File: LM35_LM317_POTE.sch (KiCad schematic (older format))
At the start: 21 parts, among them J10 TB_1X2, J6 TB_1X2, J7 TB_1X2, J8 TB_1X2, J9 TB_1X2, P4 CONN_01X03, P5 CONN_02X02, P6 CONN_01X02, P7 CONN_01X02, P8 CONN_01X02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

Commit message: Ruteo del PCB, agrego una salida de 5v y 3v en el esquematico
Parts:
- J10: value TB_1X2 -> PotO.Out
- J6: value TB_1X2 -> V.RegOut
- J7: value TB_1X2 -> Temp.Out
- J8: value TB_1X2 -> C.RegOut
- J9: value TB_1X2 -> PotTOut
- P4: value CONN_01X03 -> Pot2_Out
- P5: value CONN_02X02 -> C.reg.in
- P6: value CONN_01X02 -> V_regOut
- P7: value CONN_01X02 -> Temp_Out
- P8: value CONN_01X02 -> C_RegOut
- P9: value CONN_01X03 -> PotO_Out
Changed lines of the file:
@@
 $EndComp
 $Comp
-L GND #PWR028
+L GND #PWR031
 U 1 1 581A256F
 P 4800 1450
-F 0 "#PWR028" H 4800 1200 50  0001 C CNN
+F 0 "#PWR031" H 4800 1200 50  0001 C CNN
 F 1 "GND" H 4800 1300 50  0000 C CNN
 F 2 "" H 4800 1450 50  0000 C CNN
@@
 P 5150 1350
 F 0 "P8" H 5150 1500 50  0000 C CNN
-F 1 "CONN_01X02" V 5250 1350 50  0000 C CNN
+F 1 "C_RegOut" V 5250 1350 50  0000 C CNN
 F 2 "Pin_Headers:Pin_Header_Straight_1x02" H 5150 1350 50  0001 C CNN
 F 3 "" H 5150 1350 50  0000 C CNN
@@
 P 1850 1250
 F 0 "P5" H 1850 1400 50  0000 C CNN
-F 1 "CONN_02X02" H 1850 1100 50  0000 C CNN
+F 1 "C.reg.in" H 1850 1100 50  0000 C CNN
 F 2 "Pin_Headers:Pin_Header_Straight_2x02" H 1850 50  50  0001 C CNN
 F 3 "" H 1850 50  50  0000 C CNN
@@
 $EndComp
 $Comp
-L +5V #PWR029
+L +5V #PWR032
 U 1 1 581A2572
 P 1300 1000
-F 0 "#PWR029" H 1300 850 50  0001 C CNN
+F 0 "#PWR032" H 1300 850 50  0001 C CNN
 F 1 "+5V" H 1300 1140 50  0000 C CNN
 F 2 "" H 1300 1000 50  0000 C CNN
@@
 $EndComp
 $Comp
-L +3.3V-RESCUE-ciaa-nxp #PWR030
+L +3.3V-RESCUE-ciaa-nxp #PWR033
 U 1 1 581A2573
 P 950 1000
-F 0 "#PWR030" H 950 850 50  0001 C CNN
+F 0 "#PWR033" H 950 850 50  0001 C CNN
 F 1 "+3.3V" H 950 1140 50  0000 C CNN
 F 2 "" H 950 1000 50  0000 C CNN
@@
 $EndComp
 $Comp
-L GND #PWR031
+L GND #PWR034
 U 1 1 581A2577
 P 4400 3500
-F 0 "#PWR031" H 4400 3250 50  0001 C CNN
+F 0 "#PWR034" H 4400 3250 50  0001 C CNN
 F 1 "GND" H 4400 3350 50  0000 C CNN
 F 2 "" H 4400 3500 50  0000 C CNN
@@
 P 4750 3400
 F 0 "P6" H 4750 3550 50  0000 C CNN
-F 1 "CONN_01X02" V 4850 3400 50  0000 C CNN
+F 1 "V_regOut" V 4850 3400 50  0000 C CNN
 F 2 "Pin_Headers:Pin_Header_Straight_1x02" H 4750 3400 50  0001 C CNN
 F 3 "" H 4750 3400 50  0000 C CNN
@@
 $EndComp
 $Comp
-L +5V #PWR032
+L +5V #PWR035
 U 1 1 581A2579
 P 1700 3150
-F 0 "#PWR032" H 1700 3000 50  0001 C CNN
+F 0 "#PWR035" H 1700 3000 50  0001 C CNN
 F 1 "+5V" H 1700 3290 50  0000 C CNN
 F 2 "" H 1700 3150 50  0000 C CNN
@@
 $EndComp
 $Comp
-L GND #PWR033
+L GND #PWR036
 U 1 1 581A257B
 P 3700 4650
-F 0 "#PWR033" H 3700 4400 50  0001 C CNN
+F 0 "#PWR036" H 3700 4400 50  0001 C CNN
 F 1 "GND" H 3700 4500 50  0000 C CNN
 F 2 "" H 3700 4650 50  0000 C CNN
@@
 P 5600 3400
 F 0 "J6" H 5600 3700 60  0000 C CNN
-F 1 "TB_1X2" H 5650 3100 60  0000 C CNN
+F 1 "V.RegOut" H 5650 3100 60  0000 C CNN
 F 2 "Connect:AK300-2" H 5550 3450 60  0001 C CNN
 F 3 "" H 5550 3450 60  0000 C CNN
@@
 $EndComp
 $Comp
-L GND #PWR034
+L GND #PWR037
 U 1 1 581A257D
 P 5100 3550
-F 0 "#PWR034" H 5100 3300 50  0001 C CNN
+F 0 "#PWR037" H 5100 3300 50  0001 C CNN
 F 1 "GND" H 5100 3400 50  0000 C CNN
 F 2 "" H 5100 3550 50  0000 C CNN
@@
 P 6150 1250
 F 0 "J8" H 6150 1550 60  0000 C CNN
-F 1 "TB_1X2" H 6200 950 60  0000 C CNN
+F 1 "C.RegOut" H 6200 950 60  0000 C CNN
 F 2 "Connect:AK300-2" H 6100 1300 60  0001 C CNN
 F 3 "" H 6100 1300 60  0000 C CNN
@@
 $EndComp
 $Comp
-L GND #PWR035
+L GND #PWR038
 U 1 1 581A257F
-P 5650 1400
-F 0 "#PWR035" H 5650 1150 50  0001 C CNN
-F 1 "GND" H 5650 1250 50  0000 C CNN
-F 2 "" H 5650 1400 50  0000 C CNN
-F 3 "" H 5650 1400 50  0000 C CNN
-	1    5650 1400
+P 5700 1200
+F 0 "#PWR038" H 5700 950 50  0001 C CNN
+F 1 "GND" H 5550 1150 50  0000 C CNN
+F 2 "" H 5700 1200 50  0000 C CNN
+F 3 "" H 5700 1200 50  0000 C CNN
+	1    5700 1200
 	1    0    0    -1
 $EndComp
@@
 P 9700 4600
 F 0 "J10" H 9700 4900 60  0000 C CNN
-F 1 "TB_1X2" H 9750 4300 60  0000 C CNN
+F 1 "PotO.Out" H 9750 4300 60  0000 C CNN
 F 2 "Connect:AK300-2" H 9650 4650 60  0001 C CNN
 F 3 "" H 9650 4650 60  0000 C CNN
@@
 $EndComp
 $Comp
-L +5V #PWR036
+L +5V #PWR039
 U 1 1 581A2587
 P 1950 5900
-F 0 "#PWR036" H 1950 5750 50  0001 C CNN
+F 0 "#PWR039" H 1950 5750 50  0001 C CNN
 F 1 "+5V" H 1950 6040 50  0000 C CNN
 F 2 "" H 1950 5900 50  0000 C CNN
@@
 $EndComp
 $Comp
-L GND #PWR037
+L GND #PWR040
 U 1 1 581A2589
 P 3150 6550
-F 0 "#PWR037" H 3150 6300 50  0001 C CNN
+F 0 "#PWR040" H 3150 6300 50  0001 C CNN
 F 1 "GND" H 3150 6400 50  0000 C CNN
 F 2 "" H 3150 6550 50  0000 C CNN
@@
 P 3500 6450
 F 0 "P7" H 3500 6600 50  0000 C CNN
-F 1 "CONN_01X02" V 3600 6450 50  0000 C CNN
+F 1 "Temp_Out" V 3600 6450 50  0000 C CNN
 F 2 "Pin_Headers:Pin_Header_Straight_1x02" H 3500 6450 50  0001 C CNN
 F 3 "" H 3500 6450 50  0000 C CNN
@@
 P 4350 6450
 F 0 "J7" H 4350 6750 60  0000 C CNN
-F 1 "TB_1X2" H 4400 6150 60  0000 C CNN
+F 1 "Temp.Out" H 4400 6150 60  0000 C CNN
 F 2 "Connect:AK300-2" H 4300 6500 60  0001 C CNN
 F 3 "" H 4300 6500 60  0000 C CNN
@@
 $EndComp
 $Comp
-L GND #PWR038
+L GND #PWR041
 U 1 1 581A258C
 P 3850 6600
-F 0 "#PWR038" H 3850 6350 50  0001 C CNN
+F 0 "#PWR041" H 3850 6350 50  0001 C CNN
 F 1 "GND" H 3850 6450 50  0000 C CNN
 F 2 "" H 3850 6600 50  0000 C CNN
@@
 $EndComp
 $Comp
-L GND #PWR039
+L GND #PWR042
 U 1 1 581A258D
 P 1950 6850
-F 0 "#PWR039" H 1950 6600 50  0001 C CNN
+F 0 "#PWR042" H 1950 6600 50  0001 C CNN
 F 1 "GND" H 1950 6700 50  0000 C CNN
 F 2 "" H 1950 6850 50  0000 C CNN
@@
 P 9000 3950
 F 0 "P9" H 9000 4150 50  0000 C CNN
-F 1 "CONN_01X03" V 9100 3950 50  0000 C CNN
+F 1 "PotO_Out" V 9100 3950 50  0000 C CNN
 F 2 "Pin_Headers:Pin_Header_Straight_1x03" H 9000 3950 50  0001 C CNN
 F 3 "" H 9000 3950 50  0000 C CNN
@@
 $EndComp
 $Comp
-L +3.3V #PWR040
+L +3.3V #PWR043
 U 1 1 58207E1D
 P 8550 4050
-F 0 "#PWR040" H 8550 4010 30  0001 C CNN
+F 0 "#PWR043" H 8550 4010 30  0001 C CNN
 F 1 "+3.3V" H 8550 4160 30  0000 C CNN
 F 2 "" H 8550 4050 60  0000 C CNN
@@
 $EndComp
 $Comp
-L +5V #PWR041
+L +5V #PWR044
 U 1 1 58207EC2
 P 9400 4100
-F 0 "#PWR041" H 9400 3950 50  0001 C CNN
+F 0 "#PWR044" H 9400 3950 50  0001 C CNN
 F 1 "+5V" H 9400 4240 50  0000 C CNN
 F 2 "" H 9400 4100 50  0000 C CNN
@@
 P 9700 2750
 F 0 "J9" H 9700 3050 60  0000 C CNN
-F 1 "TB_1X2" H 9750 2450 60  0000 C CNN
+F 1 "PotTOut" H 9750 2450 60  0000 C CNN
 F 2 "Connect:AK300-2" H 9650 2800 60  0001 C CNN
 F 3 "" H 9650 2800 60  0000 C CNN
@@
 P 9000 2100
 F 0 "P4" H 9000 2300 50  0000 C CNN
-F 1 "CONN_01X03" V 9100 2100 50  0000 C CNN
+F 1 "Pot2_Out" V 9100 2100 50  0000 C CNN
 F 2 "Pin_Headers:Pin_Header_Straight_1x03" H 9000 2100 50  0001 C CNN
 F 3 "" H 9000 2100 50  0000 C CNN
@@
 $EndComp
 $Comp
-L +3.3V #PWR042
+L +3.3V #PWR045
 U 1 1 58208511
 P 8550 2200
-F 0 "#PWR042" H 8550 2160 30  0001 C CNN
+F 0 "#PWR045" H 8550 2160 30  0001 C CNN
 F 1 "+3.3V" H 8550 2310 30  0000 C CNN
 F 2 "" H 8550 2200 60  0000 C CNN
@@
 $EndComp
 $Comp
-L +5V #PWR043
+L +5V #PWR046
 U 1 1 5820851A
 P 9400 2250
-F 0 "#PWR043" H 9400 2100 50  0001 C CNN
+F 0 "#PWR046" H 9400 2100 50  0001 C CNN
 F 1 "+5V" H 9400 2390 50  0000 C CNN
 F 2 "" H 9400 2250 50  0000 C CNN
@@
 	5100 3500 5100 3550
 Wire Wire Line
-	4900 1000 5800 1000
-Wire Wire Line
-	5800 1000 5800 1150
-Wire Wire Line
-	5800 1350 5650 1350
-Wire Wire Line
-	5650 1350 5650 1400
+	4900 1000 5250 1000
 Wire Wire Line
 	4900 1300 4900 1000
@@
 Text Notes 5000 2100 0    60   Italic 0
 Iout=Vref/(R6+Pot)\nVref=1,25V aprox.
-Text Label 5550 1000 0    60   ~ 0
+Text Label 5000 1000 0    60   ~ 0
 Iout
 Text Notes 4500 4550 0    60   ~ 0
@@
 Text Label 3950 3350 0    60   ~ 0
 Vout
+Wire Wire Line
+	5800 1150 5700 1150
+Wire Wire Line
+	5700 1150 5700 1200
+Wire Wire Line
+	5800 1350 5600 1350
+Text Label 5650 1350 0    60   ~ 0
+Iout
 $EndSCHEMATC

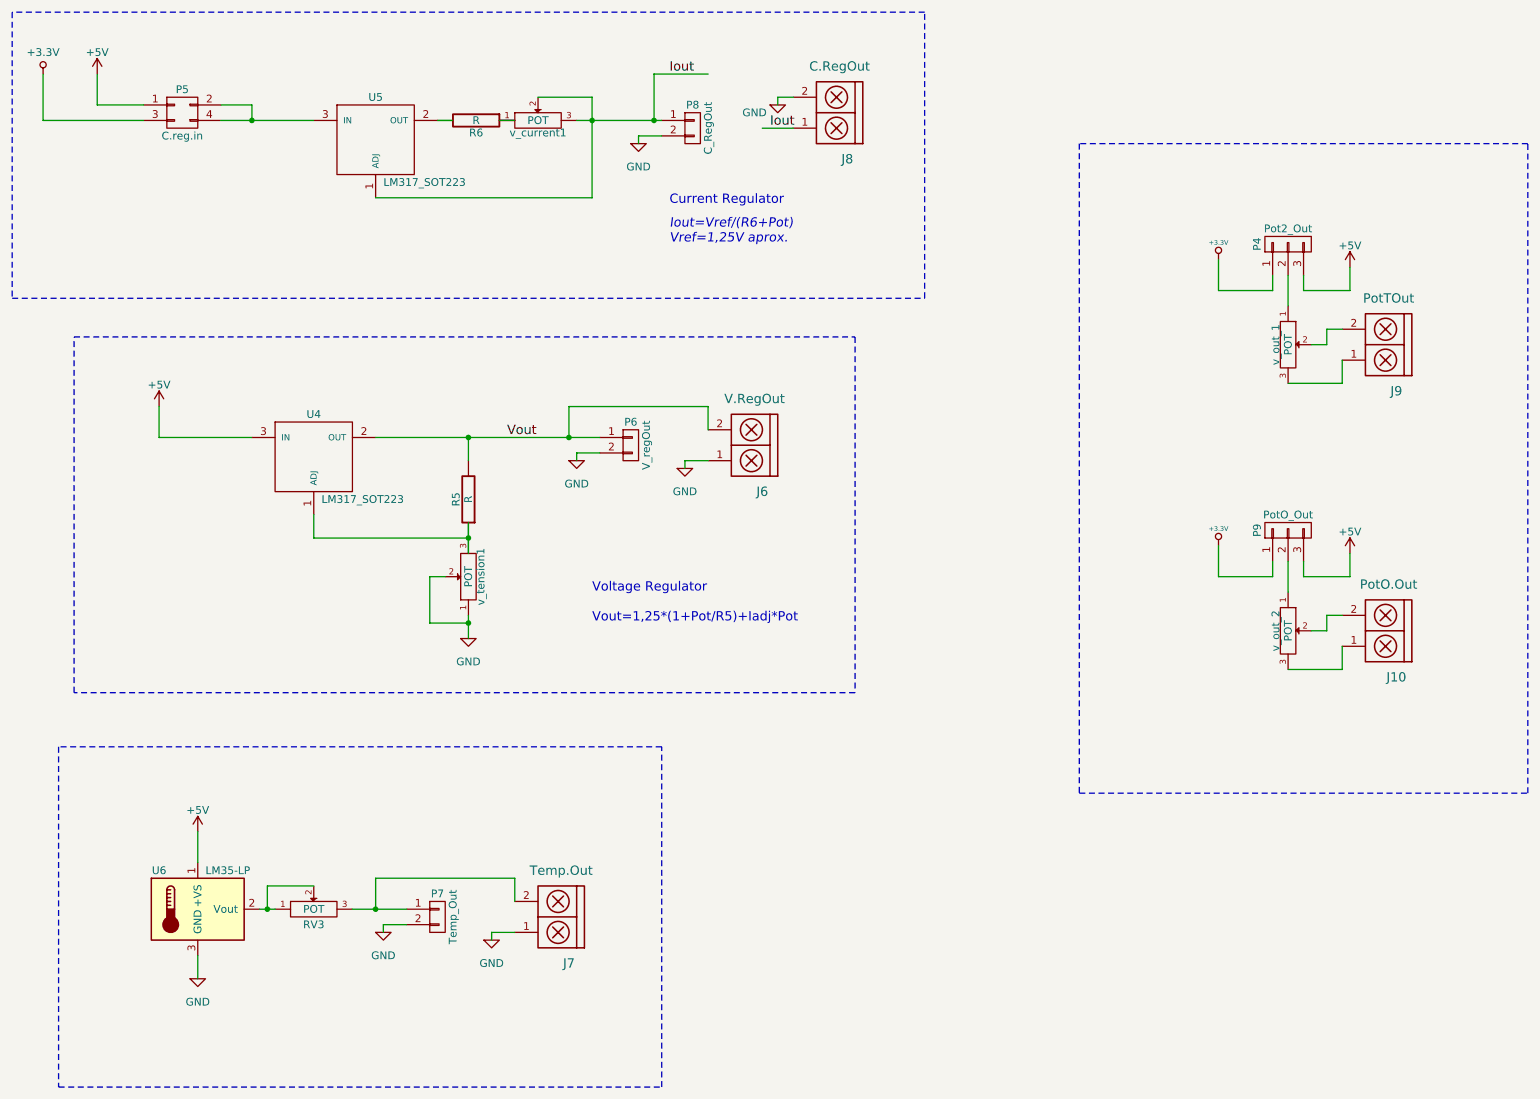
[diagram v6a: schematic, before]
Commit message: Add digikey code and comment schematic.
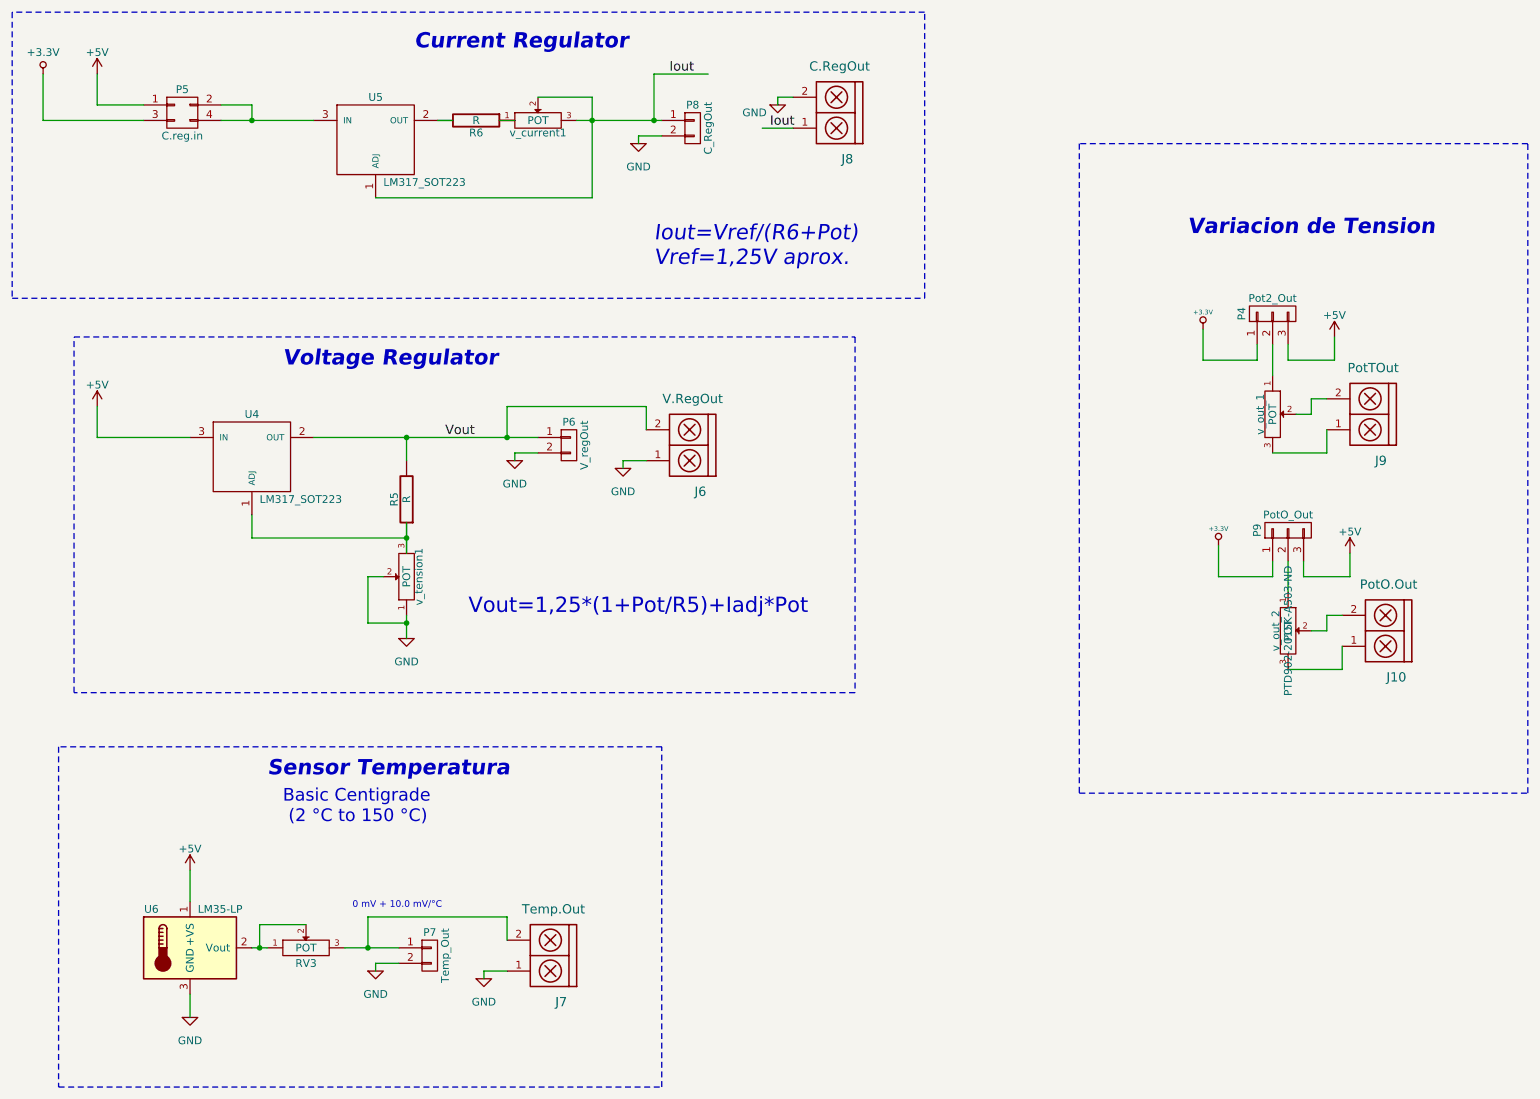
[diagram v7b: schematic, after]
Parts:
- RV3: Digikey# (none) -> A105870-ND
- U4, U5: Digikey# (none) -> LM317TFS-ND
- U6: Digikey# (none) -> LM35DZ/NOPB-ND
- v_current1, v_out_1, v_out_2, v_tension1: Digikey# (none) -> PTD902-2015K-A503-ND
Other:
- note added: "0 mV + 10.0 mV/°C"
- note added: "Basic Centigrade \n (2 °C to 150 °C)\n"
- note added: "Sensor Temperatura"
- note added: "Variacion de Tension\n"
- note added: "Voltage Regulator"
- note added: "Vout=1,25*(1+Pot/R5)+Iadj*Pot"
- note removed: "Voltage Regulator\n\nVout=1,25*(1+Pot/R5)+Iadj*Pot"
- moved on the sheet: J6, J7, J9, P4, P6, P7, R5, RV3, U4, U6, v_out_1, v_tension1
